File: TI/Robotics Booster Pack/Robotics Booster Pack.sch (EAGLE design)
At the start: 91 parts, among them U1 TPS62177.DQC, U11 SCHA4B0400, U13 XBEE-1XBEE-1_LOCK, U14 TPS5450, U3 DRV8800, U4 DRV8800, U5 DRV8800, U6 DRV8800, U7 PCA9557.RGV, U8 MPU-6050, U9 INA220.DGS

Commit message: Part placement ~90% completed. Started routing. Pin mapping figured out (for the most part).
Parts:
- removed C12, C20, C38, C6, C9: .1uF, standardparts:CAPACITOR.0603
- removed C5, C7: 1uF, standardparts:CAPACITOR.0603
- removed LED1, LED2, LED6, LED7, LED8: (no value), standardparts:LED.0603
- removed U$8: STELLARIS-LAUNCHPADSTELLARIS-LAUNCHPAD-XL, StellarisLaunchPad_Fred:STELLARIS-LAUNCHPADSTELLARIS-LAUNCHPAD-XL
- removed U7: PCA9557.RGV, packages(ti):PCA9557.RGV
- added J3, J4: (no value), solderjumper:SOLDERJUMPER.2.LRG
- added U2: PCA9538.RGV, packages(ti):PCA9538.RGV
- U13: value XBEE-1XBEE-1_LOCK -> XBEE-1B3; device SparkFun-RF:XBEE-1XBEE-1_LOCK -> SparkFun-RF:XBEE-1B3
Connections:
- removed net AD0: U$8.PD2
- removed net AD1: U$8.PD3
- removed net AD2: U$8.PE0
- removed net AD3: U$8.PE1
- removed net AD4: U$8.PE2
- removed net AD5: U$8.PE3
- removed net I2C.SCL: R6.2, U$8.PB2, U7.SCL, U8.SCL, U9.SCL
- removed net I2C.SDA: R7.2, U$8.PB3, U7.SDA, U8.SDA, U9.SDA
- removed net M0.DIR: U$8.PC4, U5.PHASE
- removed net M0.SPD: U$8.PA7, U5.ENABLE
- removed net M1.DIR: U$8.PC7, U6.PHASE
- removed net M1.SPD: U$8.PA6, U6.ENABLE
- removed net M2.DIR: U$8.PF0, U3.PHASE
- removed net M2.SPD: U$8.PD1, U3.ENABLE
- removed net M3.DIR: U$8.PF4, U4.PHASE
- removed net M3.SPD: U$8.PD0, U4.ENABLE
- removed net N$10: LED2.1
- removed net N$11: LED1.1
- removed net N$14: LED8.2
- removed net N$5: LED1.2
- removed net N$8: LED2.2
- removed net N$9: LED7.2
- removed net QEI0.A: U$8.PD6
- removed net QEI0.B: U$8.PD7
- removed net QEI1.A: U$8.PC5
- removed net QEI1.B: U$8.PC6
- removed net SPI.!CS: U$8.PA3, U11.!CS!/NC
- removed net SPI.MISO: U$8.PA4, U11.MISO/DAT0
- removed net SPI.MOSI: U$8.PA5, U11.MOSI/CMD
- removed net SPI.SCLK: U$8.PA2, U11.CLK
- removed net SVRO0: U$8.PB6
- removed net SVRO1: U$8.PB7
- removed net SVRO2: U$8.PB4
- removed net SVRO3: U$8.PB5
- removed net SVRO4: U$8.PE4
- removed net SVRO5: U$8.PE5
- removed net UART1.RXI: U$8.PB0
- removed net UART1.TXO: U$8.PB1
- net !RST: now also U2.!RST; no longer U$8.RST, U7.!RST
- net 3.3V: now also C3.+, U2.VCC; no longer C12.1, C20.1, C38.1, C5.1, C6.1, C7.1, C9.1, U$8.3.3V, U7.VCC
- net 5.0V: no longer U$8.VBUS
- net FET0.G: now also U2.P6; no longer U7.P2
- net FET1.G: now also U2.P7; no longer U7.P3
- net GND: now also C3.-, U2.A0, U2.A1, U2.GND; no longer C12.2, C20.2, C38.2, C5.2, C6.2, C7.2, C9.2, U$8.GND1, U$8.GND2, U7.A0, U7.A1, U7.A2, U7.GND
- net IMU.INT: now also U2.P5; no longer U7.P1
- net M0.EN: now also U2.P3; no longer U7.P4
- net M1.EN: now also U2.P2; no longer U7.P5
- net M2.EN: now also U2.P1; no longer U7.P6
- net M3.EN: now also U2.P0; no longer U7.P7
- net PA2: now also U11.!CS!/NC
- net PA3: now also U11.CLK
- net PA4: now also U11.MISO/DAT0
- net PA5: now also U11.MOSI/CMD
- net PA6: now also U6.ENABLE
- net PA7: now also U5.ENABLE
- net PB0: now also J3.1
- net PB1: now also J4.1
- net PB2: now also R6.2, U2.SCL, U8.SCL, U9.SCL
- net PB3: now also R7.2, U2.SDA, U8.SDA, U9.SDA
- net PC4: now also U5.PHASE
- net PC7: now also U3.PHASE
- net PD0: now also U4.ENABLE
- net PD1: now also U3.ENABLE
- net PD2: now also H1.1, U2.!INT; no longer H4.2
- net PD3: now also H1.2; no longer H4.1
- net PE0: now also H1.3; no longer H1.4
- net PE1: now also H1.4; no longer H1.3
- net PE2: now also H4.1; no longer H1.2
- net PE3: now also H4.2; no longer H1.1
- net PF0: now also U6.PHASE
- net PF3: now also U4.PHASE
- net XBEE.ASSOCIATE: no longer LED6.1
- net XBEE.CONNECTED: now also U2.P4; no longer U7.P0
- net XBEE.RSSI: no longer LED5.1
- net XBEE.RXI: now also J3.2
- net XBEE.TXO: now also J4.2
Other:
- note added: "A2 - SPI_SCLK A3 - SPI_CS A4 - SPI_MISO A5 - SPI_MOSI"
- note added: "B0 - UART1_RXI B1 - UART1_TXO B2 - I2C0_SCL B3 - I2C0_SDA"
- note added: "D2 - AIN5 D3 - AIN4 E0 - AIN3 E1 - AIN2"
- note added: "E2 - AIN1 E3 - AIN0 A6 - M1_Speed A7 - M0_Speed"
- note added: "PC4 - M0_Direction PF0 - M1_Direction PC7 - M2_Direction PF4 - M3_Direction PD2 - !INT"
- note added: "QEI0_A - D6 QEI0_B - D7 QEI1_A - C5 QEI1_B - C6"
- note added: "Servo0 - B6 Servo1 - B7 Servo2 - B4 Servo3 - B5"
- note added: "Servo4 - E4 Servo5 - E5 M3_Speed - D0 M2_Speed - D1"
- note added: "TODO: - Add UART1 and I2C0 headers - Finish deciding on final layout of board - Figure out how to map power to headers"
- note removed: "TODO: - Apply Pin Map to signal names - Add UART1 and I2C0 headers - Finish deciding on final layout of board - Figure out how to map power to headers"
- moved on the sheet: C22, C3, C4, C41, C42, C8, D3, D4, D6, H1, H10, H11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

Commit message: Part placement is mostly complete for RBP v3. Layout coming along. Routing multiple Power Header Options will be difficult...
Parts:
- removed LED5: (no value), standardparts:LED.0603
- removed U$21, U$4: HOLE.4MM, screw_holes:HOLE.4MM
- added H21, H22: 1X4, headers(.1in):1X4
- added H23: 1X2, headers(.1in):1X2
- added J10, J11, J12, J13, J14, J15, J16, J17, J18, J19, J6, J7, J8, J9: (no value), solderjumper:SOLDERJUMPER.2.LRG
- added J20: (no value), solderjumper:SOLDERJUMPER.3.LRG.12
- added LED0, LED1, LED2: (no value), standardparts:LED.0603
- added R2, R4: 1k, standardparts:RESISTOR.0603
- added R3: 1.5k, standardparts:RESISTOR.0603
- J5: device solderjumper:SOLDERJUMPER.2.LRG -> solderjumper:SOLDERJUMPER.3.LRG
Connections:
- removed net N$66: H11.1, H11.2, H11.3, H11.4
- removed net N$67: H14.1, H14.2, H14.3, H14.4
- removed net N$68: H17.1, H17.2, H17.3, H17.4
- removed net N$69: H2.1, H2.2, H2.3, H2.4
- removed net N$70: H5.1, H5.2, H5.3, H5.4
- removed net N$71: H8.1, H8.2, H8.3, H8.4
- removed net N$72: C10.+, C28.1, C29.1, U5.VMOT, U6.VMOT
- removed net N$73: C11.+, C30.1, C31.1, U3.VMOT, U4.VMOT
- removed net XBEE.ASSOCIATE: U13.DIO5
- removed net XBEE.RSSI: U13.RSSI
- removed net XBEE.RXI: J3.2, U13.DOUT
- removed net XBEE.TXO: J4.2, U13.DIN
- new net N$2: LED0.2, R2.1
- new net N$3: LED1.2, R3.1
- new net N$4: R4.1, U13.DIO9
- new net N$5: H23.1, J5.3
- new net V1: H2.1, H2.2, H2.3, H2.4, J1.2, J2.2, J3.2
- new net V2: H5.1, H5.2, H5.3, H5.4, J4.2, J6.2, J7.2
- new net V3: H8.1, H8.2, H8.3, H8.4, J10.2, J8.2, J9.2
- new net V4: H11.1, H11.2, H11.3, H11.4, J11.2, J12.2, J13.2
- new net V5: H14.1, H14.2, H14.3, H14.4, J14.2, J15.2, J16.2
- new net V6: H17.1, H17.2, H17.3, H17.4, J17.2, J18.2, J19.2
- new net VMOTOR: C10.+, C11.+, C28.1, C29.1, C30.1, C31.1, J20.2, U3.VMOT, U4.VMOT, U5.VMOT, U6.VMOT
- net 3.3V: now also H21.1, H22.1, J10.1, J13.1, J16.1, J19.1, J3.1, J7.1, LED0.1
- net 5.0V: now also J12.1, J15.1, J18.1, J2.1, J20.3, J6.1, J9.1, LED1.1
- net GND: now also H21.2, H22.2, H23.2, LED2.2, R2.2, R3.2
- net PB0: now also H21.3, U13.DOUT; no longer J3.1
- net PB1: now also H21.4, U13.DIN; no longer J4.1
- net PB2: now also H22.4
- net PB3: now also H22.3
- net VBAT: now also J1.1, J11.1, J14.1, J17.1, J20.1, J4.1, J5.1, J8.1
- net VFET: now also J5.2
- net XBEE.CONNECTED: now also LED2.1, R4.2; no longer U13.DIO3
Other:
- note added: "M0_Direction - PC4 M1_Direction - PF0 M2_Direction - PC7 M3_Direction - PF4 !INT! - PD2"
- note added: "TODO: - Figure out how to map power to headers - Route everything..."
- note removed: "PC4 - M0_Direction PF0 - M1_Direction PC7 - M2_Direction PF4 - M3_Direction PD2 - !INT"
- note removed: "TODO: - Add UART1 and I2C0 headers - Finish deciding on final layout of board - Figure out how to map power to headers"
- moved on the sheet: C10, C11, C17, C19, C2, C21, C22, C23, C24, C25, C26, C27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

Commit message: More routing. Completed Motor Controller power traces and 3.3v & 5v regulator power traces.
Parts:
- C2: device standardparts:CAPACITOR.1206 -> standardparts:CAPACITOR.0603
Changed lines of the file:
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@@
 <part name="U$65" library="microbuilder" deviceset="3.3V" device=""/>
 <part name="U$10" library="microbuilder" deviceset="GND" device=""/>
-<part name="C2" library="standardparts" deviceset="CAPACITOR" device=".1206" value="2.2uF"/>
+<part name="C2" library="standardparts" deviceset="CAPACITOR" device=".0603" value="2.2uF"/>
 <part name="C4" library="standardparts" deviceset="CAPACITOR" device=".0805" value="22uF"/>
 <part name="H31" library="te-connectivity" deviceset="1X3" device=".4DB"/>

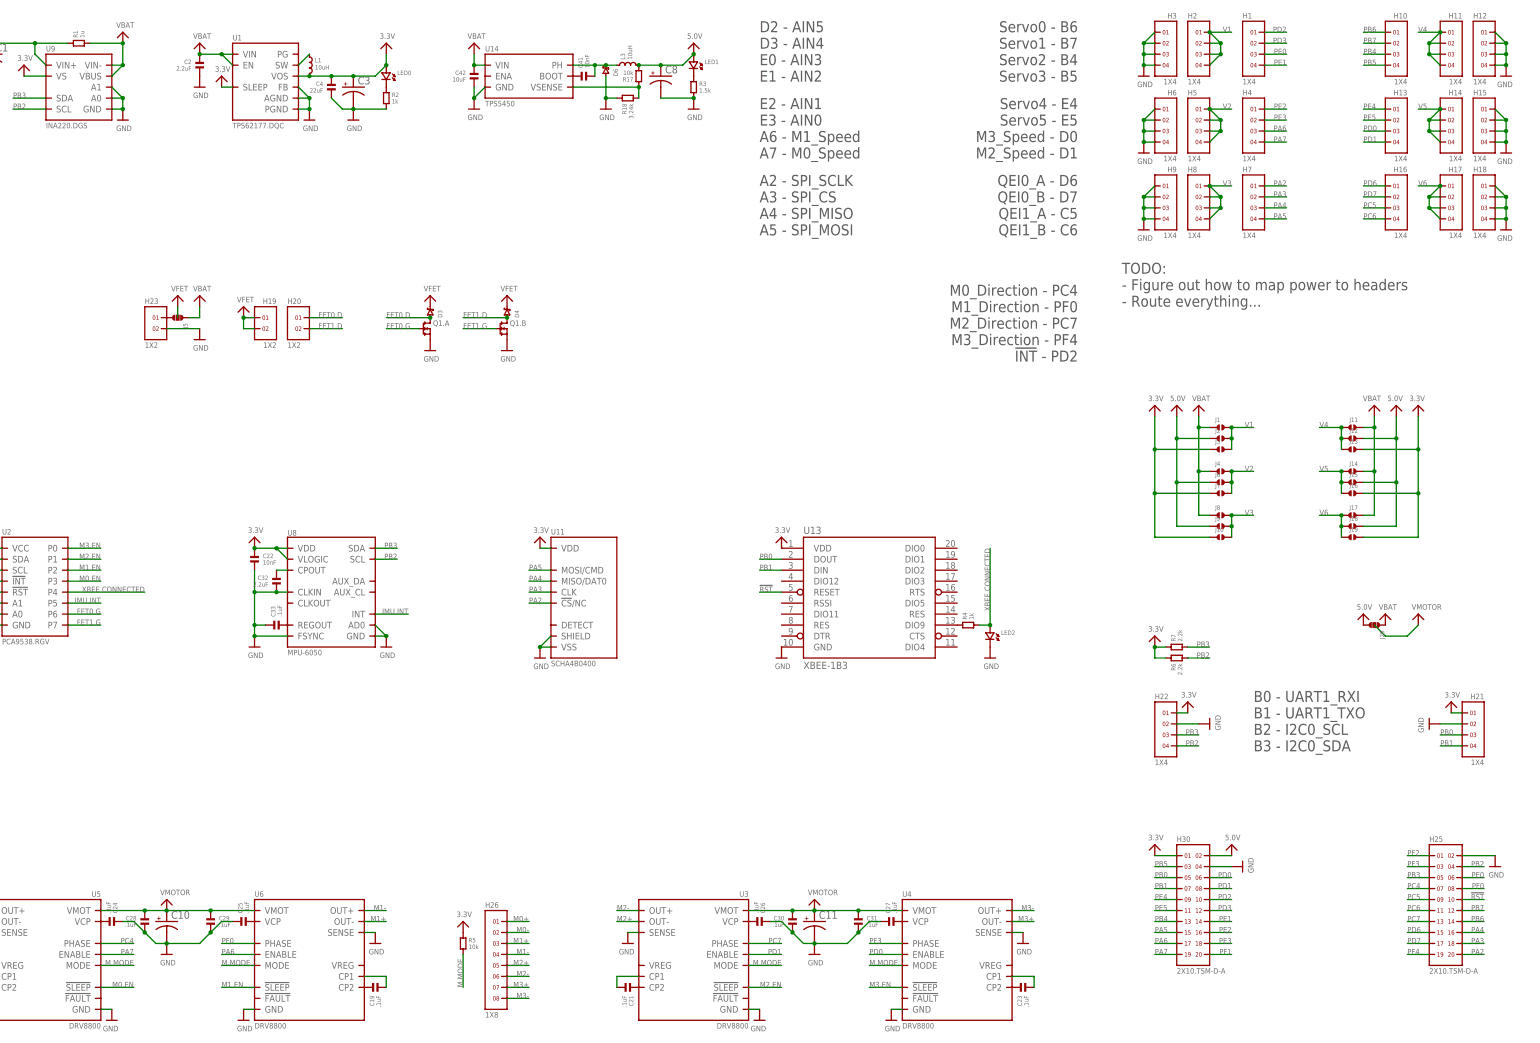
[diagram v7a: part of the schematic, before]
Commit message: More routing fun! Got a significant amount ofpower signals rounted. Replaced 1W 1mOhm power resistor with 3W 0.5mOhm resistor (able to carry much more current)
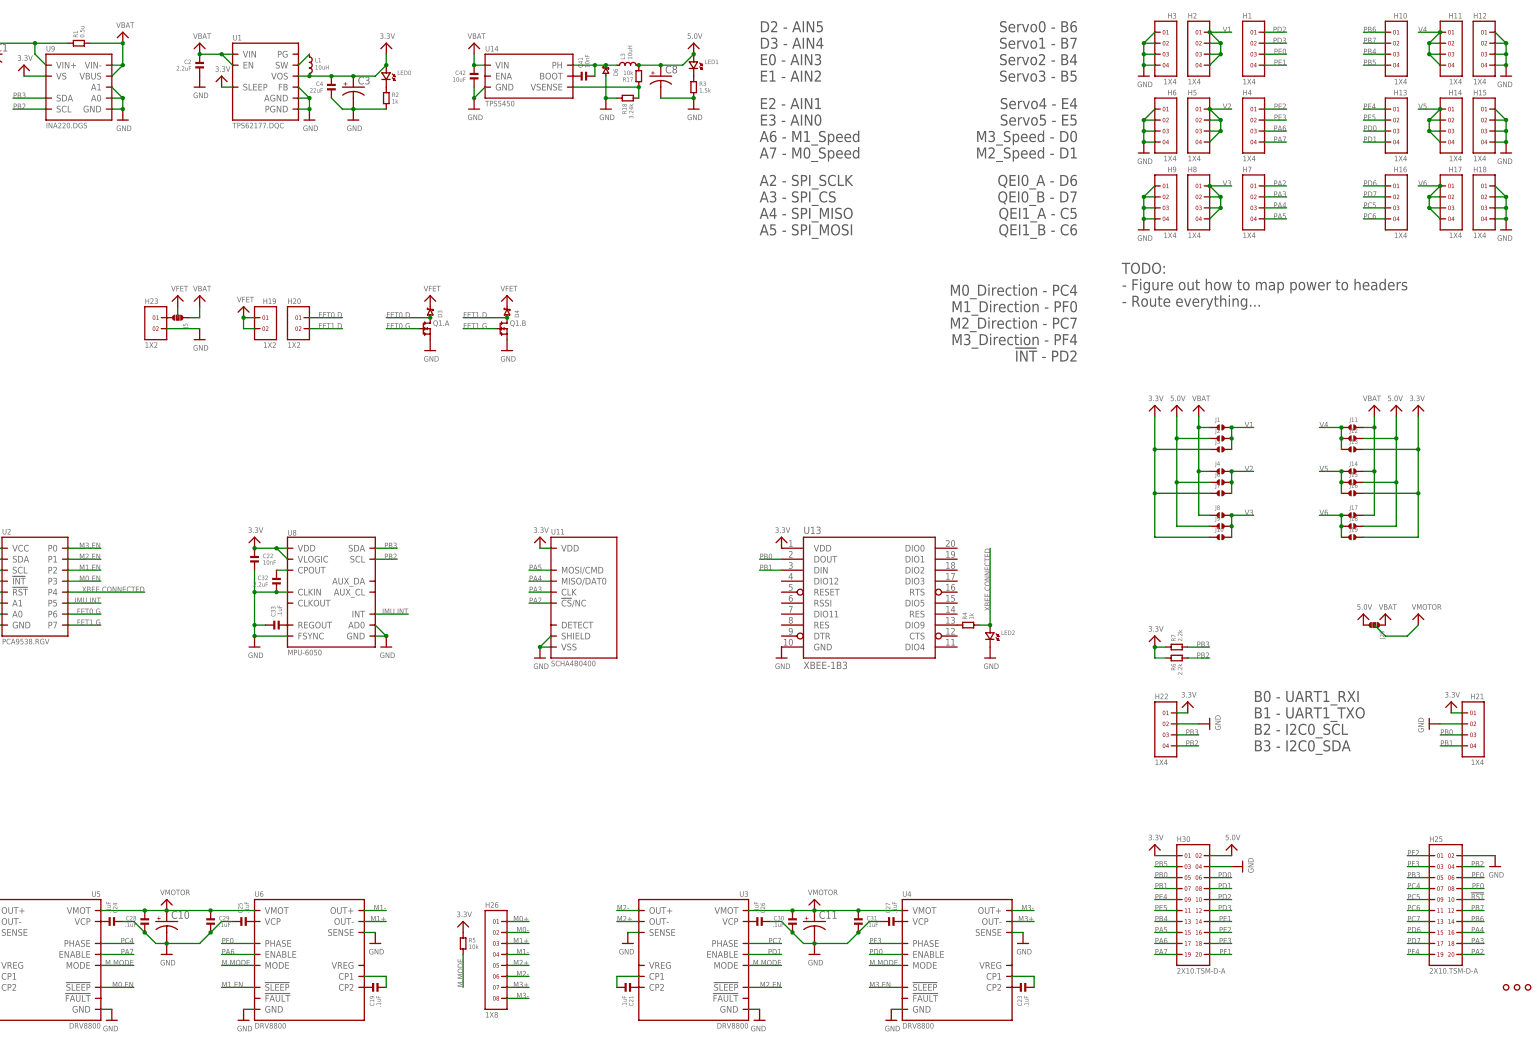
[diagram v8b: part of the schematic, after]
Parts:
- added U$21, U$3, U$4: HOLE.4MM, screw_holes:HOLE.4MM
- R1: value 1u -> 0.5u; device vishay:RESISTOR.WSK -> tt-electronics:RESISTOR.2512
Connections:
- net !RST: no longer U13.RESET
